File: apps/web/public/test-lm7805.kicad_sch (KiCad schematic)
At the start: 5 parts, among them J1 VIN_CONN, J2 VOUT_5V, U1 LM7805

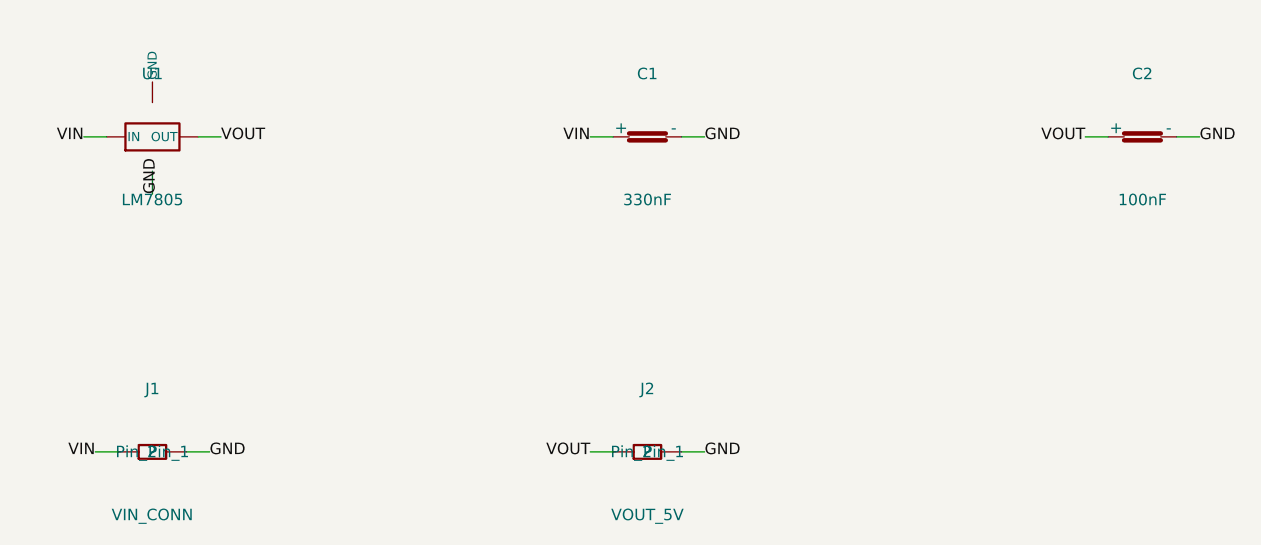
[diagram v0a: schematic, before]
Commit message: fix: remove title_h padding to eliminate empty space at bottom of schematic
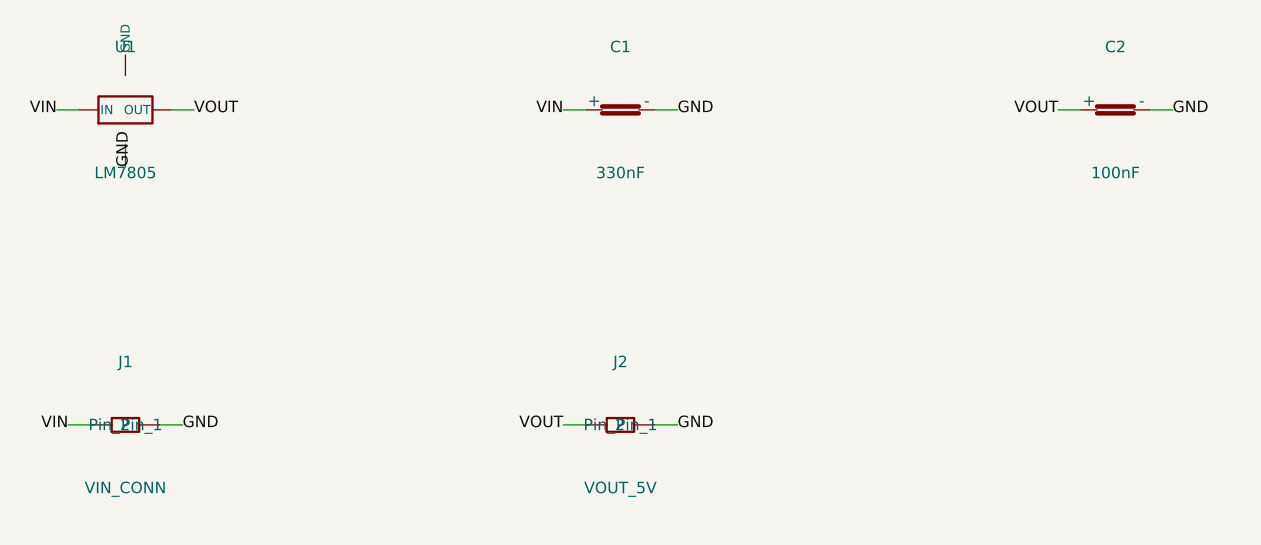
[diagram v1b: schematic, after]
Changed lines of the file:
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@@
 (kicad_sch (version 20230121) (generator "layrix-circuit-synth")
-  (paper "User" 168 107)
-  (symbol (lib_id "Device:VReg_3Pin") (at 15 15 0) (unit 1) (in_bom yes) (on_board yes)
-    (property "Reference" "U1" (at 15 8 0) (effects (font (size 1.27 1.27)) (justify center)))
-    (property "Value" "LM7805" (at 15 22 0) (effects (font (size 1.27 1.27)) (justify center)))
-    (property "Footprint" "Package_TO_SOT_THT:TO-220-3_Vertical" (at 15 25 0) (effects (font (size 1.27 1.27)) (hide yes)))
+  (paper "User" 162 79)
+  (symbol (lib_id "Device:VReg_3Pin") (at 12 12 0) (unit 1) (in_bom yes) (on_board yes)
+    (property "Reference" "U1" (at 12 5 0) (effects (font (size 1.27 1.27)) (justify center)))
+    (property "Value" "LM7805" (at 12 19 0) (effects (font (size 1.27 1.27)) (justify center)))
+    (property "Footprint" "Package_TO_SOT_THT:TO-220-3_Vertical" (at 12 22 0) (effects (font (size 1.27 1.27)) (hide yes)))
   )
-  (symbol (lib_id "Device:C") (at 70 15 0) (unit 1) (in_bom yes) (on_board yes)
-    (property "Reference" "C1" (at 70 8 0) (effects (font (size 1.27 1.27)) (justify center)))
-    (property "Value" "330nF" (at 70 22 0) (effects (font (size 1.27 1.27)) (justify center)))
-    (property "Footprint" "Capacitor_THT:C_Disc_D5.0mm_W2.5mm_P5.00mm" (at 70 25 0) (effects (font (size 1.27 1.27)) (hide yes)))
+  (symbol (lib_id "Device:C") (at 67 12 0) (unit 1) (in_bom yes) (on_board yes)
+    (property "Reference" "C1" (at 67 5 0) (effects (font (size 1.27 1.27)) (justify center)))
+    (property "Value" "330nF" (at 67 19 0) (effects (font (size 1.27 1.27)) (justify center)))
+    (property "Footprint" "Capacitor_THT:C_Disc_D5.0mm_W2.5mm_P5.00mm" (at 67 22 0) (effects (font (size 1.27 1.27)) (hide yes)))
   )
-  (symbol (lib_id "Device:C") (at 125 15 0) (unit 1) (in_bom yes) (on_board yes)
-    (property "Reference" "C2" (at 125 8 0) (effects (font (size 1.27 1.27)) (justify center)))
-    (property "Value" "100nF" (at 125 22 0) (effects (font (size 1.27 1.27)) (justify center)))
-    (property "Footprint" "Capacitor_THT:C_Disc_D5.0mm_W2.5mm_P5.00mm" (at 125 25 0) (effects (font (size 1.27 1.27)) (hide yes)))
+  (symbol (lib_id "Device:C") (at 122 12 0) (unit 1) (in_bom yes) (on_board yes)
+    (property "Reference" "C2" (at 122 5 0) (effects (font (size 1.27 1.27)) (justify center)))
+    (property "Value" "100nF" (at 122 19 0) (effects (font (size 1.27 1.27)) (justify center)))
+    (property "Footprint" "Capacitor_THT:C_Disc_D5.0mm_W2.5mm_P5.00mm" (at 122 22 0) (effects (font (size 1.27 1.27)) (hide yes)))
   )
-  (symbol (lib_id "Connector_Generic:Conn_01x02") (at 15 50 0) (unit 1) (in_bom yes) (on_board yes)
-    (property "Reference" "J1" (at 15 43 0) (effects (font (size 1.27 1.27)) (justify center)))
-    (property "Value" "VIN_CONN" (at 15 57 0) (effects (font (size 1.27 1.27)) (justify center)))
-    (property "Footprint" "Connector_PinHeader_2.54mm:PinHeader_1x02_P2.54mm_Vertical" (at 15 60 0) (effects (font (size 1.27 1.27)) (hide yes)))
+  (symbol (lib_id "Connector_Generic:Conn_01x02") (at 12 47 0) (unit 1) (in_bom yes) (on_board yes)
+    (property "Reference" "J1" (at 12 40 0) (effects (font (size 1.27 1.27)) (justify center)))
+    (property "Value" "VIN_CONN" (at 12 54 0) (effects (font (size 1.27 1.27)) (justify center)))
+    (property "Footprint" "Connector_PinHeader_2.54mm:PinHeader_1x02_P2.54mm_Vertical" (at 12 57 0) (effects (font (size 1.27 1.27)) (hide yes)))
   )
-  (symbol (lib_id "Connector_Generic:Conn_01x02") (at 70 50 0) (unit 1) (in_bom yes) (on_board yes)
-    (property "Reference" "J2" (at 70 43 0) (effects (font (size 1.27 1.27)) (justify center)))
-    (property "Value" "VOUT_5V" (at 70 57 0) (effects (font (size 1.27 1.27)) (justify center)))
-    (property "Footprint" "Connector_PinHeader_2.54mm:PinHeader_1x02_P2.54mm_Vertical" (at 70 60 0) (effects (font (size 1.27 1.27)) (hide yes)))
+  (symbol (lib_id "Connector_Generic:Conn_01x02") (at 67 47 0) (unit 1) (in_bom yes) (on_board yes)
+    (property "Reference" "J2" (at 67 40 0) (effects (font (size 1.27 1.27)) (justify center)))
+    (property "Value" "VOUT_5V" (at 67 54 0) (effects (font (size 1.27 1.27)) (justify center)))
+    (property "Footprint" "Connector_PinHeader_2.54mm:PinHeader_1x02_P2.54mm_Vertical" (at 67 57 0) (effects (font (size 1.27 1.27)) (hide yes)))
   )
-  (wire (pts (xy 9.92 15.0) (xy 7.38 15.0)) (stroke (width 0.1524) (type default)))
-  (label "VIN" (at 7.38 15.0 180) (effects (font (size 1.27 1.27))))
-  (wire (pts (xy 66.19 15.0) (xy 63.65 15.0)) (stroke (width 0.1524) (type default)))
-  (label "VIN" (at 63.65 15.0 180) (effects (font (size 1.27 1.27))))
-  (wire (pts (xy 11.19 50.0) (xy 8.65 50.0)) (stroke (width 0.1524) (type default)))
-  (label "VIN" (at 8.65 50.0 180) (effects (font (size 1.27 1.27))))
-  (wire (pts (xy 15.0 18.81) (xy 15.0 21.35)) (stroke (width 0.1524) (type default)))
-  (label "GND" (at 15.0 21.35 90) (effects (font (size 1.27 1.27))))
-  (wire (pts (xy 73.81 15.0) (xy 76.35 15.0)) (stroke (width 0.1524) (type default)))
-  (label "GND" (at 76.35 15.0 0) (effects (font (size 1.27 1.27))))
-  (wire (pts (xy 128.81 15.0) (xy 131.35 15.0)) (stroke (width 0.1524) (type default)))
-  (label "GND" (at 131.35 15.0 0) (effects (font (size 1.27 1.27))))
-  (wire (pts (xy 18.81 50.0) (xy 21.35 50.0)) (stroke (width 0.1524) (type default)))
-  (label "GND" (at 21.35 50.0 0) (effects (font (size 1.27 1.27))))
-  (wire (pts (xy 73.81 50.0) (xy 76.35 50.0)) (stroke (width 0.1524) (type default)))
-  (label "GND" (at 76.35 50.0 0) (effects (font (size 1.27 1.27))))
-  (wire (pts (xy 20.08 15.0) (xy 22.62 15.0)) (stroke (width 0.1524) (type default)))
-  (label "VOUT" (at 22.62 15.0 0) (effects (font (size 1.27 1.27))))
-  (wire (pts (xy 121.19 15.0) (xy 118.65 15.0)) (stroke (width 0.1524) (type default)))
-  (label "VOUT" (at 118.65 15.0 180) (effects (font (size 1.27 1.27))))
-  (wire (pts (xy 66.19 50.0) (xy 63.65 50.0)) (stroke (width 0.1524) (type default)))
-  (label "VOUT" (at 63.65 50.0 180) (effects (font (size 1.27 1.27))))
+  (wire (pts (xy 6.92 12.0) (xy 4.38 12.0)) (stroke (width 0.1524) (type default)))
+  (label "VIN" (at 4.38 12.0 180) (effects (font (size 1.27 1.27))))
+  (wire (pts (xy 63.19 12.0) (xy 60.65 12.0)) (stroke (width 0.1524) (type default)))
+  (label "VIN" (at 60.65 12.0 180) (effects (font (size 1.27 1.27))))
+  (wire (pts (xy 8.19 47.0) (xy 5.65 47.0)) (stroke (width 0.1524) (type default)))
+  (label "VIN" (at 5.65 47.0 180) (effects (font (size 1.27 1.27))))
+  (wire (pts (xy 12.0 15.81) (xy 12.0 18.35)) (stroke (width 0.1524) (type default)))
+  (label "GND" (at 12.0 18.35 90) (effects (font (size 1.27 1.27))))
+  (wire (pts (xy 70.81 12.0) (xy 73.35 12.0)) (stroke (width 0.1524) (type default)))
+  (label "GND" (at 73.35 12.0 0) (effects (font (size 1.27 1.27))))
+  (wire (pts (xy 125.81 12.0) (xy 128.35 12.0)) (stroke (width 0.1524) (type default)))
+  (label "GND" (at 128.35 12.0 0) (effects (font (size 1.27 1.27))))
+  (wire (pts (xy 15.81 47.0) (xy 18.35 47.0)) (stroke (width 0.1524) (type default)))
+  (label "GND" (at 18.35 47.0 0) (effects (font (size 1.27 1.27))))
+  (wire (pts (xy 70.81 47.0) (xy 73.35 47.0)) (stroke (width 0.1524) (type default)))
+  (label "GND" (at 73.35 47.0 0) (effects (font (size 1.27 1.27))))
+  (wire (pts (xy 17.08 12.0) (xy 19.62 12.0)) (stroke (width 0.1524) (type default)))
+  (label "VOUT" (at 19.62 12.0 0) (effects (font (size 1.27 1.27))))
+  (wire (pts (xy 118.19 12.0) (xy 115.65 12.0)) (stroke (width 0.1524) (type default)))
+  (label "VOUT" (at 115.65 12.0 180) (effects (font (size 1.27 1.27))))
+  (wire (pts (xy 63.19 47.0) (xy 60.65 47.0)) (stroke (width 0.1524) (type default)))
+  (label "VOUT" (at 60.65 47.0 180) (effects (font (size 1.27 1.27))))
   (sheet_instances (path "/" (page "1")))
 )
